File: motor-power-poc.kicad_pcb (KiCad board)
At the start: 4 copper layers, 150 parts, among them J1 Conn_01x04_Pin, J2 USB_C_Receptacle_USB2.0_14P, J3 Conn_01x02, J4 Conn_02x02_Counter_Clockwise, J5 Conn_02x06_Counter_Clockwise, M1 Motor_Servo, M2 Motor_Servo, M3 DC, Q1 Q_NMOS, Q10 Q_NMOS, Q2 Q_NMOS, Q3 Q_NMOS, Q4 Q_NMOS, Q5 Q_NMOS, Q6 Q_NMOS, Q7 Q_NMOS, Q8 Q_NMOS, Q9 Q_NMOS, SW1 SW_Push, SW2 SW_Push, U1 QRE1113GR, U10 CJ431, U11 DRV8701, U2 QRE1113GR, U3 QRE1113GR, U4 ESP32-S3FH4R2, U5 LM74502, U6 TPS5430DDA, U7 TPS56A37, U8 TPS2121, U9 LDL212PV33R, Y1 48M

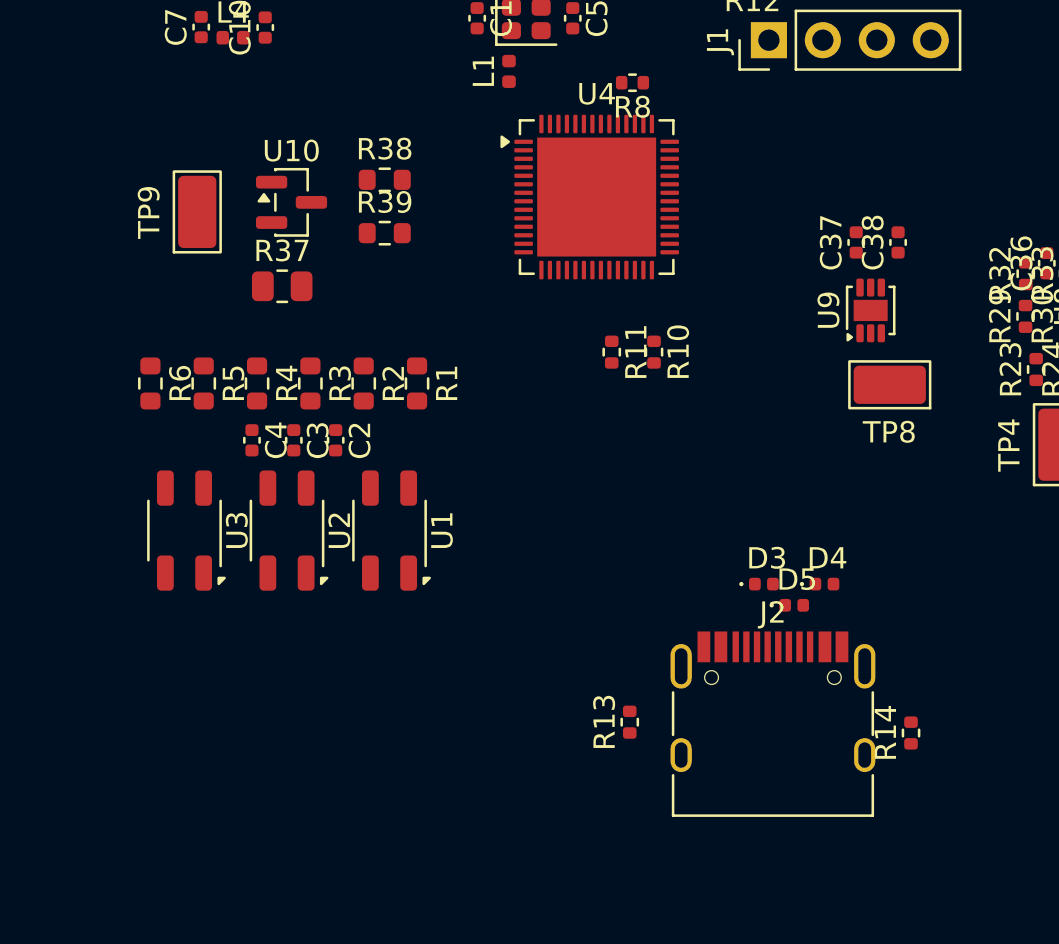
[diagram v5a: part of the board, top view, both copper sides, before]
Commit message: pcb: add 3v3 and 3v layout
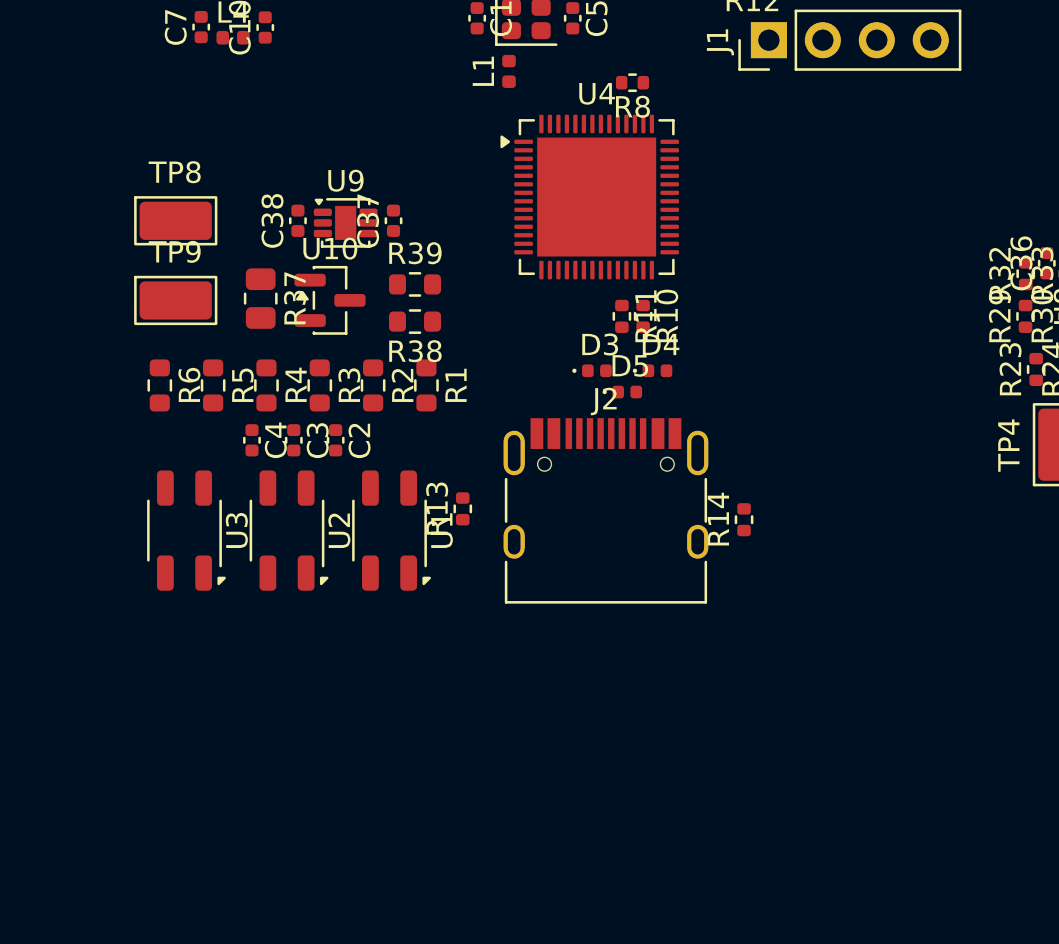
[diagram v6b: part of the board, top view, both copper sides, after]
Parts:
- moved TP8 34.5 mm to (114.0, 86.0), turned to 0 degrees
- moved C38 28.3 mm to (119.8, 86.0)
- moved U9 25.1 mm to (122.0, 86.1), turned to 0 degrees
- moved C37 21.8 mm to (124.2, 86.0)
- moved R14 12.8 mm to (140.8, 100.1)
- moved D3 12.8 mm to (133.8, 93.1)
- moved D5 12.8 mm to (135.2, 94.1)
- moved J2 12.8 mm to (134.2, 100.1)
- moved R13 12.8 mm to (127.5, 99.6)
- moved D4 12.8 mm to (136.7, 93.1)
- moved R38 6.82 mm to (125.3, 90.7), turned to 180 degrees
- moved U10 4.96 mm to (121.3, 89.7)
- moved TP9 4.29 mm to (114.0, 89.8), turned to 0 degrees
- moved R39 2.80 mm to (125.3, 89.0)
- moved R10 1.76 mm to (136.0, 90.5)
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
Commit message: pcb: add QR113 layout
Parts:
- moved R3 7.32 mm to (113.5, 94.5)
- moved R4 6.77 mm to (125.0, 94.5), turned to 90 degrees
- moved R2 5.10 mm to (118.2, 94.5)
- moved R5 4.55 mm to (120.2, 94.5), turned to 90 degrees
- moved C4 3.14 mm to (114.5, 97.0), turned to 0 degrees
- moved R1 2.90 mm to (123.0, 94.5)
- moved C2 2.56 mm to (124.0, 97.0), turned to 0 degrees
- moved R6 2.37 mm to (115.5, 94.5), turned to 90 degrees
- moved C3 0.73 mm to (119.2, 97.0), turned to 0 degrees
- moved U3 0.19 mm to (114.5, 100.8)
- moved U1 0.18 mm to (124.0, 100.8)
- moved U2 0.17 mm to (119.2, 100.8)

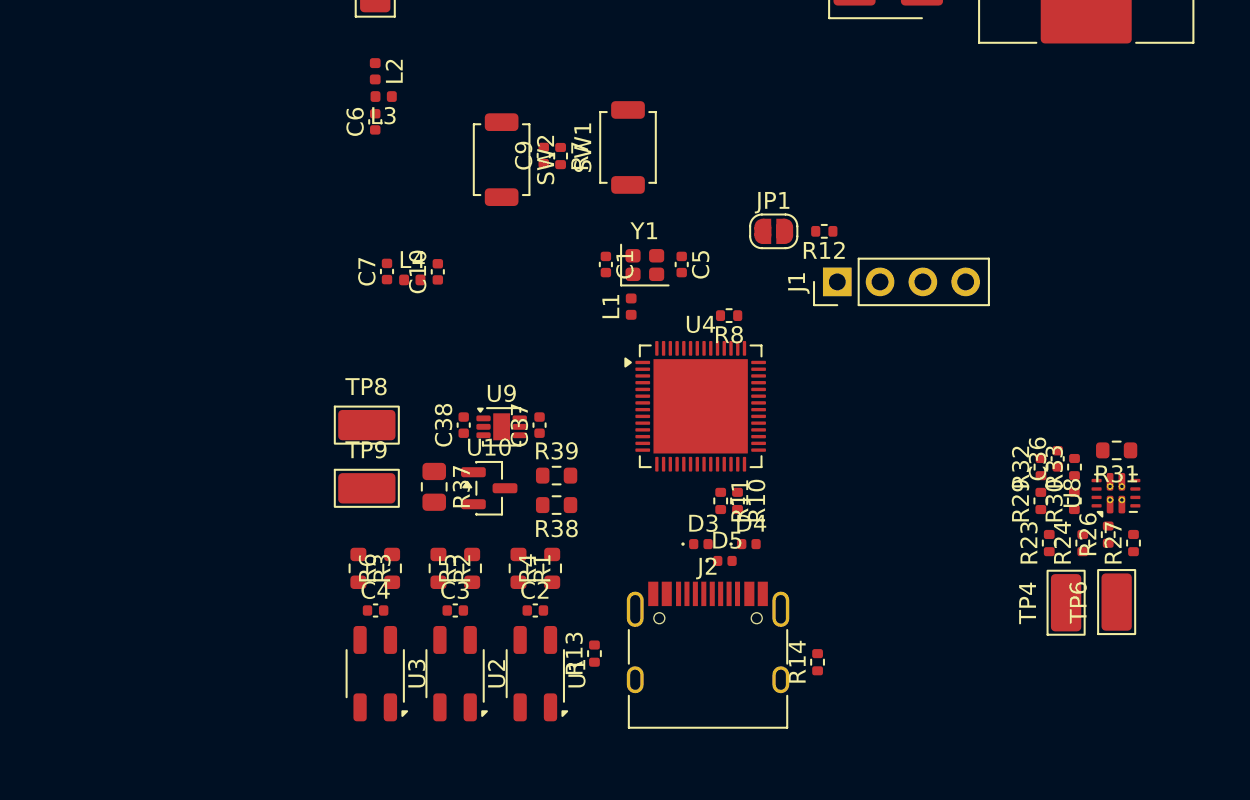
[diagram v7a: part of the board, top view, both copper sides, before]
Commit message: pcb: add TPS2121 layout
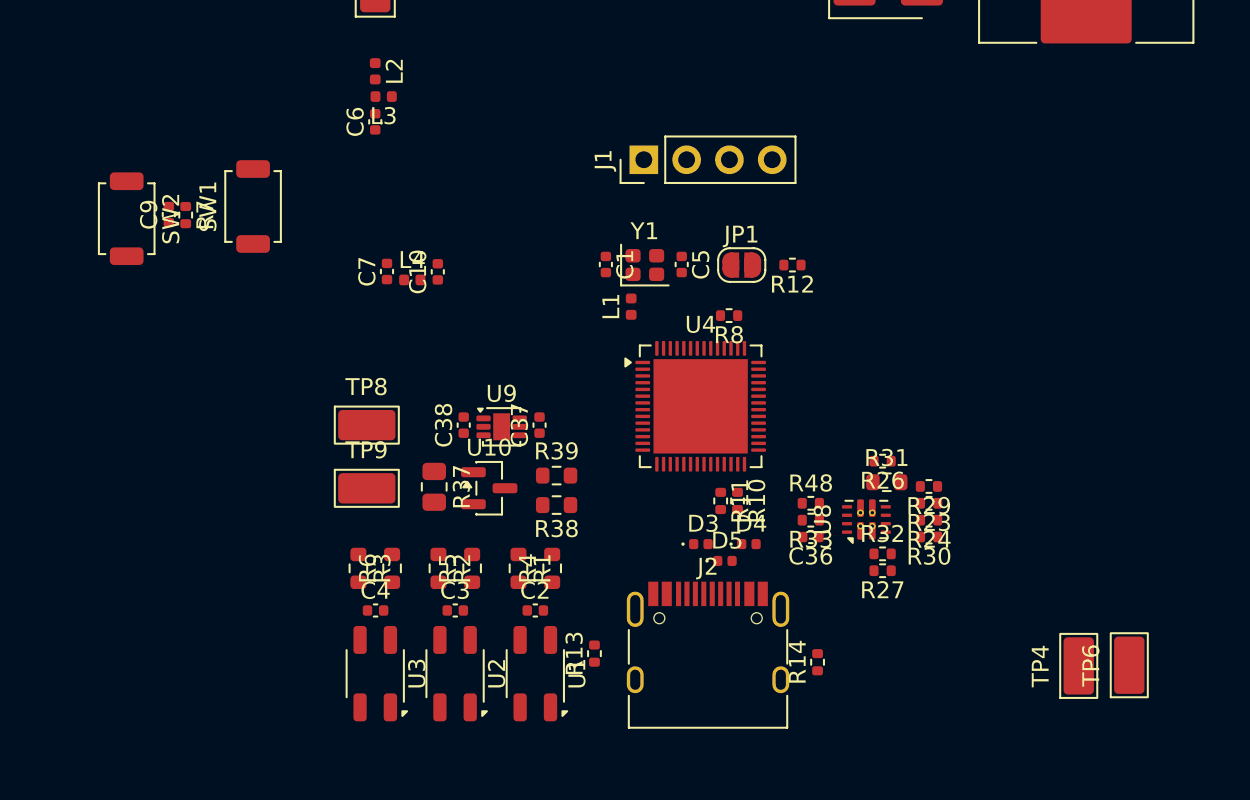
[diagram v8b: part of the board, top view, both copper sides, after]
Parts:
- added R48: 10k, Resistor_SMD:R_0402_1005Metric, F.Cu at (140.3, 90.6)
- moved C9 22.5 mm to (102.2, 73.5)
- moved R7 22.5 mm to (103.2, 73.5)
- moved SW1 22.5 mm to (107.2, 73.0)
- moved SW2 22.5 mm to (99.8, 73.8)
- moved R33 16.0 mm to (140.3, 91.6), turned to 180 degrees
- moved C36 15.4 mm to (140.3, 92.6), turned to 180 degrees
- moved R27 15.0 mm to (144.6, 94.6), turned to 180 degrees
- moved U8 14.9 mm to (143.7, 91.6)
- moved R26 14.1 mm to (144.6, 88.1), turned to 180 degrees
- moved R31 13.8 mm to (144.9, 89.4), turned to 0 degrees
- moved J1 13.6 mm to (130.4, 70.2)
- moved R32 10.7 mm to (144.6, 93.6), turned to 0 degrees
- moved R24 9.22 mm to (147.4, 91.6), turned to 180 degrees
- moved R30 8.88 mm to (147.4, 92.6), turned to 180 degrees
- moved R23 7.51 mm to (147.4, 90.6), turned to 180 degrees
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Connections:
- U4 pad 37: unconnected-(U4-SPICLK_P/GPIO47-Pad37) -> ST
- U8 pad 9: GND -> ST
